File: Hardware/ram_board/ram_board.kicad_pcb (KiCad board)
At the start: 2 copper layers, 80.8 x 60.1 mm, 17 parts, among them J1 Conn_01x40, U1 74HC00, U2 74HC04, U3 IS61C5128AL-10TLI, U4 74HC02, U5 74HC273

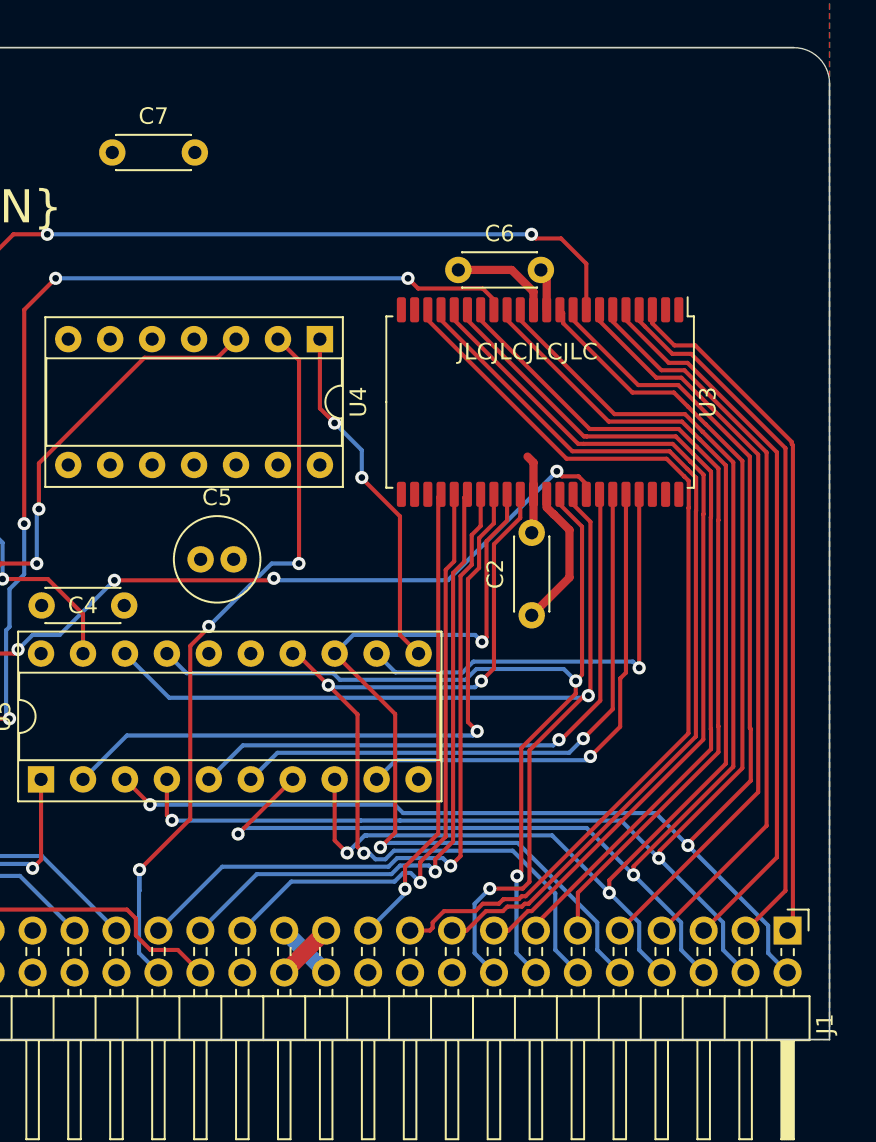
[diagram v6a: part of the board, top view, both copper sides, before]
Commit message: Can load intel hex files + jump to arbitrary address
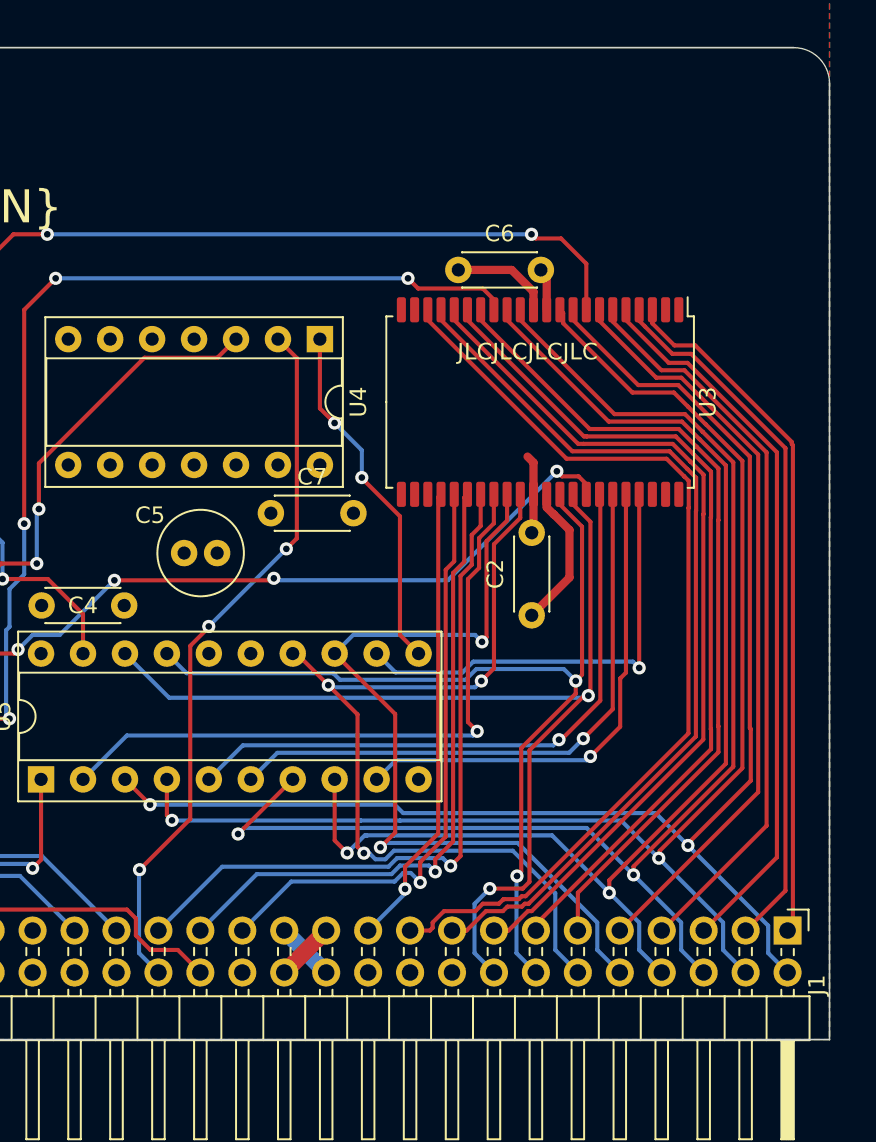
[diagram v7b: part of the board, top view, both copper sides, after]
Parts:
- moved C7 23.9 mm to (155.5, 106.7)
- moved C5 1.07 mm to (150.3, 109.1)
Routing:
- net ~{SLOT_SEL}: track 45.7 -> 43.2 mm
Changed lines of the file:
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@@
     (property "ki_keywords" "connector")
     (attr through_hole)
-    (fp_text reference "J1" (at 5.655 -2.27 90) (layer "F.SilkS")
+    (fp_text reference "J1" (at 3.302 -1.778 90) (layer "F.SilkS")
         (effects (font (size 1 1) (thickness 0.15)))
     )
@@
   )
   (footprint "Capacitor_THT:C_Radial_D5.0mm_H11.0mm_P2.00mm" (layer "F.Cu")
-    (at 151.273 109.474)
+    (at 150.273 109.093)
     (descr "C, Radial series, Radial, pin pitch=2.00mm, diameter=5mm, height=11mm, Non-Polar Electrolytic Capacitor")
     (tags "C Radial series Radial pin pitch 2.00mm diameter 5mm height 11mm Non-Polar Electrolytic Capacitor")
@@
     (property "ki_keywords" "cap capacitor")
     (attr through_hole)
-    (fp_text reference "C5" (at 1 -3.75) (layer "F.SilkS")
+    (fp_text reference "C5" (at -2.064 -2.286) (layer "F.SilkS")
         (effects (font (size 1 1) (thickness 0.15)))
     )
@@
   )
   (footprint "Capacitor_THT:C_Disc_D4.3mm_W1.9mm_P5.00mm" (layer "F.Cu")
-    (at 145.923 84.836)
+    (at 155.528 106.68)
     (descr "C, Disc series, Radial, pin pitch=5.00mm, , diameter*width=4.3*1.9mm^2, Capacitor, http://www.vishay.com/docs/45233/krseries.pdf")
     (tags "C Disc series Radial pin pitch 5.00mm  diameter 4.3mm width 1.9mm Capacitor")
@@
   (segment (start 123.548 109.725) (end 123.548 100.81) (width 0.25) (layer "B.Cu") (net 39))
   (segment (start 131.146676 129.622676) (end 131.146676 128.9945) (width 0.25) (layer "B.Cu") (net 39))
-  (segment (start 157.226 109.728) (end 157.232577 109.721423) (width 0.25) (layer "F.Cu") (net 44))
   (segment (start 150.645 114.713009) (end 151.765 113.593009) (width 0.25) (layer "F.Cu") (net 44))
-  (segment (start 157.232577 109.734577) (end 157.226 109.728) (width 0.25) (layer "F.Cu") (net 44))
   (segment (start 147.574 128.270002) (end 150.645 125.199002) (width 0.25) (layer "F.Cu") (net 44))
-  (segment (start 157.232577 109.721423) (end 157.232577 97.415577) (width 0.25) (layer "F.Cu") (net 44))
-  (segment (start 151.765 113.593009) (end 151.765 113.538) (width 0.25) (layer "F.Cu") (net 44))
-  (segment (start 157.232577 97.415577) (end 155.956 96.139) (width 0.25) (layer "F.Cu") (net 44))
+  (segment (start 155.956 96.139) (end 157.099 97.282) (width 0.25) (layer "F.Cu") (net 44))
+  (segment (start 157.099 97.282) (end 157.099 108.204) (width 0.25) (layer "F.Cu") (net 44))
   (segment (start 150.645 125.199002) (end 150.645 114.713009) (width 0.25) (layer "F.Cu") (net 44))
-  (segment (start 151.765 113.538) (end 151.820009 113.538) (width 0.25) (layer "F.Cu") (net 44))
-  (via (at 157.226 109.728) (size 0.8) (drill 0.4) (layers "F.Cu" "B.Cu") (net 44))
+  (segment (start 157.099 108.204) (end 156.464 108.839) (width 0.25) (layer "F.Cu") (net 44))
+  (via (at 156.464 108.839) (size 0.8) (drill 0.4) (layers "F.Cu" "B.Cu") (net 44))
   (via (at 147.574 128.270002) (size 0.8) (drill 0.4) (layers "F.Cu" "B.Cu") (net 44))
   (via (at 151.765 113.538) (size 0.8) (drill 0.4) (layers "F.Cu" "B.Cu") (net 44))
-  (segment (start 147.542 129.572) (end 147.574 129.54) (width 0.25) (layer "B.Cu") (net 44))
-  (segment (start 155.575 109.728) (end 157.226 109.728) (width 0.25) (layer "B.Cu") (net 44))
-  (segment (start 151.765 113.538) (end 155.575 109.728) (width 0.25) (layer "B.Cu") (net 44))
   (segment (start 148.717 134.493) (end 147.542 133.318) (width 0.25) (layer "B.Cu") (net 44))
+  (segment (start 151.765 113.538) (end 156.464 108.839) (width 0.25) (layer "B.Cu") (net 44))
   (segment (start 147.542 128.302002) (end 147.574 128.270002) (width 0.25) (layer "B.Cu") (net 44))
-  (segment (start 147.574 129.54) (end 147.574 128.270002) (width 0.25) (layer "B.Cu") (net 44))
   (segment (start 147.542 133.318) (end 147.542 128.302002) (width 0.25) (layer "B.Cu") (net 44))
   (segment (start 151.257 134.493) (end 149.892 133.128) (width 0.25) (layer "F.Cu") (net 45))
@@
   (segment (start 139.492501 118.918501) (end 139.7 119.126) (width 0.25) (layer "B.Cu") (net 51))
   (segment (start 158.496 100.33) (end 158.496 96.139) (width 0.25) (layer "F.Cu") (net 52))
-  (segment (start 160.998926 104.521) (end 160.909 104.431074) (width 0.25) (layer "F.Cu") (net 52))
   (segment (start 164.47 115.179) (end 163.345 114.054) (width 0.25) (layer "F.Cu") (net 52))
   (segment (start 159.385 101.219) (end 158.496 100.33) (width 0.25) (layer "F.Cu") (net 52))
   (segment (start 163.345 114.054) (end 163.345 106.867074) (width 0.25) (layer "F.Cu") (net 52))
-  (segment (start 161.036 104.558074) (end 161.036 104.521) (width 0.25) (layer "F.Cu") (net 52))
-  (segment (start 161.036 104.521) (end 160.998926 104.521) (width 0.25) (layer "F.Cu") (net 52))
   (segment (start 163.345 106.867074) (end 161.036 104.558074) (width 0.25) (layer "F.Cu") (net 52))
   (via (at 161.036 104.521) (size 0.8) (drill 0.4) (layers "F.Cu" "B.Cu") (net 52))
